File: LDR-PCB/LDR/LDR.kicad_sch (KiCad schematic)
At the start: 7 parts, among them J1 Conn_01x03_Socket, Q1 NPN, U1 ${SIM.PARAMS}

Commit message: LDR circuit is done nu nog plaatsen
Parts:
- removed Q1: NPN, symbol Simulation_SPICE:NPN
- added Q1: NPN, Package_TO_SOT_THT:TO-92_Inline, symbol Transistor_BJT:PN2222A
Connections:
- net +3V3: now also R2.1, Q1.3 (C)
- net GND: now also R1.2
- net OUT: now also Q1.1 (E)
- net at R1.1: now also R2.2, U1.1 (+)
- net at U1.3: now also Q1.2 (B)
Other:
- moved on the sheet: R1, R2

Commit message: Footprint toegevoegd
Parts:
- J1: footprint (none) -> Connector_PinSocket_2.00mm:PinSocket_1x03_P2.00mm_Vertical
- R2, R3, R4: footprint (none) -> Resistor_THT:R_Axial_DIN0204_L3.6mm_D1.6mm_P5.08mm_Horizontal
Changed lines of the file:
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@@
       (effects (font (size 1.27 1.27)) (justify left) hide)
     )
-    (property "Footprint" "" (at 138.43 99.568 90)
+    (property "Footprint" "Resistor_THT:R_Axial_DIN0204_L3.6mm_D1.6mm_P5.08mm_Horizontal" (at 138.43 99.568 90)
       (effects (font (size 1.27 1.27)) hide)
     )
@@
       (effects (font (size 1.27 1.27)) (justify left) hide)
     )
-    (property "Footprint" "" (at 103.505 98.425 0)
+    (property "Footprint" "Connector_PinSocket_2.00mm:PinSocket_1x03_P2.00mm_Vertical" (at 103.505 98.425 0)
       (effects (font (size 1.27 1.27)) hide)
     )
@@
       (effects (font (size 1.27 1.27)) (justify left) hide)
     )
-    (property "Footprint" "" (at 144.272 101.6 90)
+    (property "Footprint" "Resistor_THT:R_Axial_DIN0204_L3.6mm_D1.6mm_P5.08mm_Horizontal" (at 144.272 101.6 90)
       (effects (font (size 1.27 1.27)) hide)
     )
@@
       (effects (font (size 1.27 1.27)) (justify left) hide)
     )
-    (property "Footprint" "" (at 145.415 86.868 90)
-      (effects (font (size 1.27 1.27)) hide)
-    )
+    (property "Footprint" "Resistor_THT:R_Axial_DIN0204_L3.6mm_D1.6mm_P5.08mm_Horizontal" (at 145.415 86.868 90)
+      (effects (font (size 1.27 1.27)) hide)
+    )

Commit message: opamp footprint toegevoegd
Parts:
- U1: footprint (none) -> Package_DIP:DIP-6_W10.16mm
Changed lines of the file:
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@@
       (effects (font (size 1.27 1.27)) hide)
     )
-    (property "Footprint" "" (at 167.005 95.25 0)
+    (property "Footprint" "Package_DIP:DIP-6_W10.16mm" (at 167.005 95.25 0)
       (effects (font (size 1.27 1.27)) hide)
     )

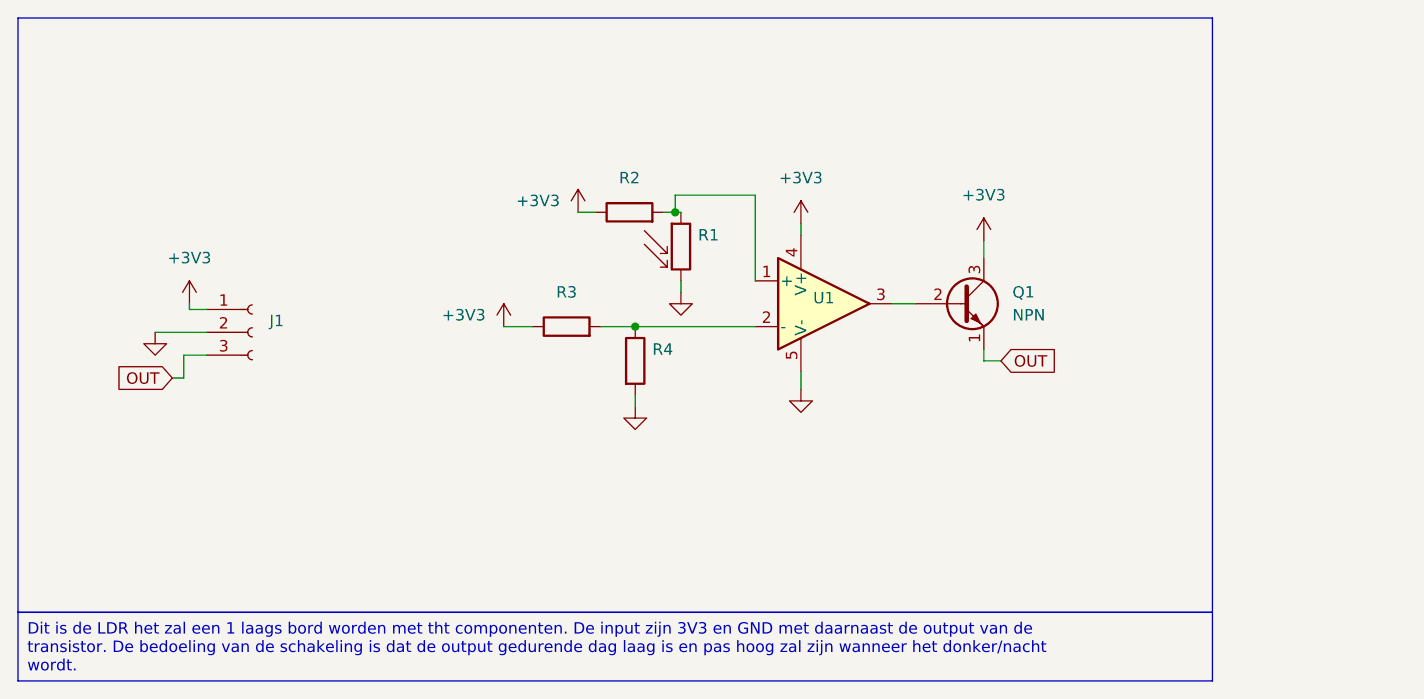
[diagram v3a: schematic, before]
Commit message: LDR zal nu de 3v3_en omlaag trekken om de pico uit te zetten
Gedeeltelijke merge
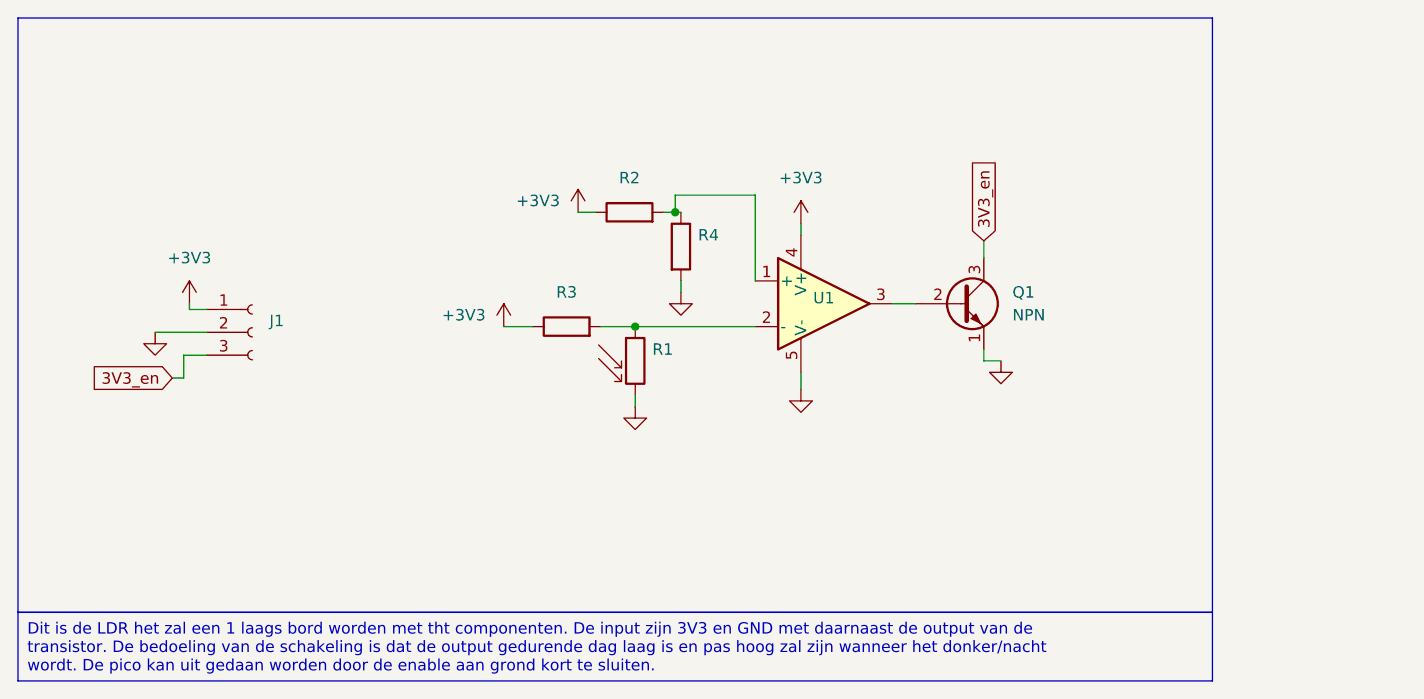
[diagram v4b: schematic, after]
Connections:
- net +3V3: no longer Q1.3 (C)
- net GND: now also Q1.1 (E)
- net at R2.2, U1.1 (+): now also R4.1; no longer R1.1
- net at R3.2, U1.2 (-): now also R1.1; no longer R4.1
- net OUT renamed 3V3_en
- net 3V3_en: now also Q1.3 (C); no longer Q1.1 (E)
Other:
- moved on the sheet: R1, R4
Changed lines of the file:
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@@
     (comment 1 "kjlhlkhlkj")
   )
+  (junction (at 150.495 85.09) (diameter 0) (color 0 0 0 0)
+  )
   (junction (at 146.05 97.79) (diameter 0) (color 0 0 0 0)
   )
-  (junction (at 150.495 85.09) (diameter 0) (color 0 0 0 0)
-  )
   (wire (pts (xy 95.885 100.965) (xy 95.885 103.505))
     (stroke (width 0) (type default))
@@
     (stroke (width 0) (type default))
   )
+  (wire (pts (xy 146.05 97.79) (xy 159.385 97.79))
+    (stroke (width 0) (type default))
+  )
   (wire (pts (xy 184.785 100.33) (xy 184.785 101.6))
     (stroke (width 0) (type default))
@@
     (stroke (width 0) (type default))
   )
-  (wire (pts (xy 146.05 97.79) (xy 159.385 97.79))
-    (stroke (width 0) (type default))
-  )
   (wire (pts (xy 150.495 85.09) (xy 151.13 85.09))
     (stroke (width 0) (type default))
@@
     (fill (type none))
   )
-  (text_box "Dit is de LDR het zal een 1 laags bord worden met tht componenten. De input zijn 3V3 en GND met daarnaast de output van de transistor. De bedoeling van de schakeling is dat de output gedurende dag laag is en pas hoog zal zijn wanneer het donker/nacht wordt."
+  (text_box "Dit is de LDR het zal een 1 laags bord worden met tht componenten. De input zijn 3V3 en GND met daarnaast de output van de transistor. De bedoeling van de schakeling is dat de output gedurende dag laag is en pas hoog zal zijn wanneer het donker/nacht wordt. De pico kan uit gedaan worden door de enable aan grond kort te sluiten."
     (at 77.47 129.54 0) (size 132.715 7.62)
     (stroke (width 0) (type default))
@@
     (effects (font (size 1.27 1.27)) (justify left top))
   )
-  (global_label "OUT" (shape input) (at 94.615 103.505 180) (fields_autoplaced)
+  (global_label "3V3_en" (shape input) (at 94.615 103.505 180) (fields_autoplaced)
     (effects (font (size 1.27 1.27)) (justify right))
-    (property "Intersheetrefs" "${INTERSHEET_REFS}" (at 88.0806 103.505 0)
+    (property "Intersheetrefs" "${INTERSHEET_REFS}" (at 84.9964 103.505 0)
       (effects (font (size 1.27 1.27)) (justify right) hide)
     )
   )
-  (global_label "OUT" (shape input) (at 186.69 101.6 0) (fields_autoplaced)
+  (global_label "3V3_en" (shape input) (at 184.785 88.265 90) (fields_autoplaced)
     (effects (font (size 1.27 1.27)) (justify left))
-    (property "Intersheetrefs" "${INTERSHEET_REFS}" (at 193.2244 101.6 0)
-      (effects (font (size 1.27 1.27)) (justify left) hide)
-    )
-  )
-  (symbol (lib_id "Device:R_Photo") (at 151.13 88.9 0) (unit 1)
-    (in_bom yes) (on_board yes) (dnp no) (fields_autoplaced)
-    (property "Reference" "R1" (at 153.035 87.63 0)
+    (property "Intersheetrefs" "${INTERSHEET_REFS}" (at 184.785 78.6464 90)
+      (effects (font (size 1.27 1.27)) (justify left) hide)
+    )
+  )
+  (symbol (lib_id "Device:R_Photo") (at 146.05 101.6 0) (unit 1)
+    (in_bom yes) (on_board yes) (dnp no) (fields_autoplaced)
+    (property "Reference" "R1" (at 147.955 100.33 0)
       (effects (font (size 1.27 1.27)) (justify left))
     )
-    (property "Value" "R_Photo" (at 153.035 90.17 0)
-      (effects (font (size 1.27 1.27)) (justify left) hide)
-    )
-    (property "Footprint" "Resistor_THT:R_Axial_DIN0204_L3.6mm_D1.6mm_P5.08mm_Horizontal" (at 152.4 95.25 90)
-      (effects (font (size 1.27 1.27)) (justify left) hide)
-    )
-    (property "Datasheet" "~" (at 151.13 90.17 0)
+    (property "Value" "R_Photo" (at 147.955 102.87 0)
+      (effects (font (size 1.27 1.27)) (justify left) hide)
+    )
+    (property "Footprint" "Resistor_THT:R_Axial_DIN0204_L3.6mm_D1.6mm_P5.08mm_Horizontal" (at 147.32 107.95 90)
+      (effects (font (size 1.27 1.27)) (justify left) hide)
+    )
+    (property "Datasheet" "~" (at 146.05 102.87 0)
       (effects (font (size 1.27 1.27)) hide)
     )
@@
     )
   )
+  (symbol (lib_id "power:GND") (at 186.69 101.6 0) (unit 1)
+    (in_bom yes) (on_board yes) (dnp no) (fields_autoplaced)
+    (property "Reference" "#PWR07" (at 186.69 107.95 0)
+      (effects (font (size 1.27 1.27)) hide)
+    )
+    (property "Value" "GND" (at 186.69 106.68 0)
+      (effects (font (size 1.27 1.27)) hide)
+    )
+    (property "Footprint" "" (at 186.69 101.6 0)
+      (effects (font (size 1.27 1.27)) hide)
+    )
+    (property "Datasheet" "" (at 186.69 101.6 0)
+      (effects (font (size 1.27 1.27)) hide)
+    )
+    (pin "1")
+    (instances
+      (project "LDR"
+        (path "/2e6b5c95-f01c-4aeb-aaa9-5aa7ab28cad0"
+          (reference "#PWR07") (unit 1)
+        )
+      )
+    )
+  )
   (symbol (lib_id "Connector:Conn_01x03_Socket") (at 103.505 98.425 0) (unit 1)
     (in_bom yes) (on_board yes) (dnp no) (fields_autoplaced)
@@
     )
   )
-  (symbol (lib_id "power:+3V3") (at 184.785 88.265 0) (unit 1)
-    (in_bom yes) (on_board yes) (dnp no) (fields_autoplaced)
-    (property "Reference" "#PWR07" (at 184.785 92.075 0)
-      (effects (font (size 1.27 1.27)) hide)
-    )
-    (property "Value" "+3V3" (at 184.785 83.185 0)
-      (effects (font (size 1.27 1.27)))
-    )
-    (property "Footprint" "" (at 184.785 88.265 0)
-      (effects (font (size 1.27 1.27)) hide)
-    )
-    (property "Datasheet" "" (at 184.785 88.265 0)
-      (effects (font (size 1.27 1.27)) hide)
-    )
-    (pin "1")
-    (instances
-      (project "LDR"
-        (path "/2e6b5c95-f01c-4aeb-aaa9-5aa7ab28cad0"
-          (reference "#PWR07") (unit 1)
-        )
-      )
-    )
-  )
-  (symbol (lib_id "Device:R") (at 146.05 101.6 0) (unit 1)
-    (in_bom yes) (on_board yes) (dnp no) (fields_autoplaced)
-    (property "Reference" "R4" (at 147.955 100.33 0)
+  (symbol (lib_id "Device:R") (at 151.13 88.9 0) (unit 1)
+    (in_bom yes) (on_board yes) (dnp no) (fields_autoplaced)
+    (property "Reference" "R4" (at 153.035 87.63 0)
       (effects (font (size 1.27 1.27)) (justify left))
     )
-    (property "Value" "R" (at 147.955 102.87 0)
-      (effects (font (size 1.27 1.27)) (justify left) hide)
-    )
-    (property "Footprint" "Resistor_THT:R_Axial_DIN0204_L3.6mm_D1.6mm_P5.08mm_Horizontal" (at 144.272 101.6 90)
-      (effects (font (size 1.27 1.27)) hide)
-    )
-    (property "Datasheet" "~" (at 146.05 101.6 0)
-      (effects (font (size 1.27 1.27)) hide)
-    )
+    (property "Value" "R" (at 153.035 90.17 0)
+      (effects (font (size 1.27 1.27)) (justify left) hide)
+    )
+    (property "Footprint" "Resistor_THT:R_Axial_DIN0204_L3.6mm_D1.6mm_P5.08mm_Horizontal" (at 149.352 88.9 90)
+      (effects (font (size 1.27 1.27)) hide)
+    )
+    (property "Datasheet" "~" (at 151.13 88.9 0)
+      (effects (font (size 1.27 1.27)) hide)
+    )
